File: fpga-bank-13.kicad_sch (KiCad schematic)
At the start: 1 part, among them U1 XC7K410T-2FFG900I

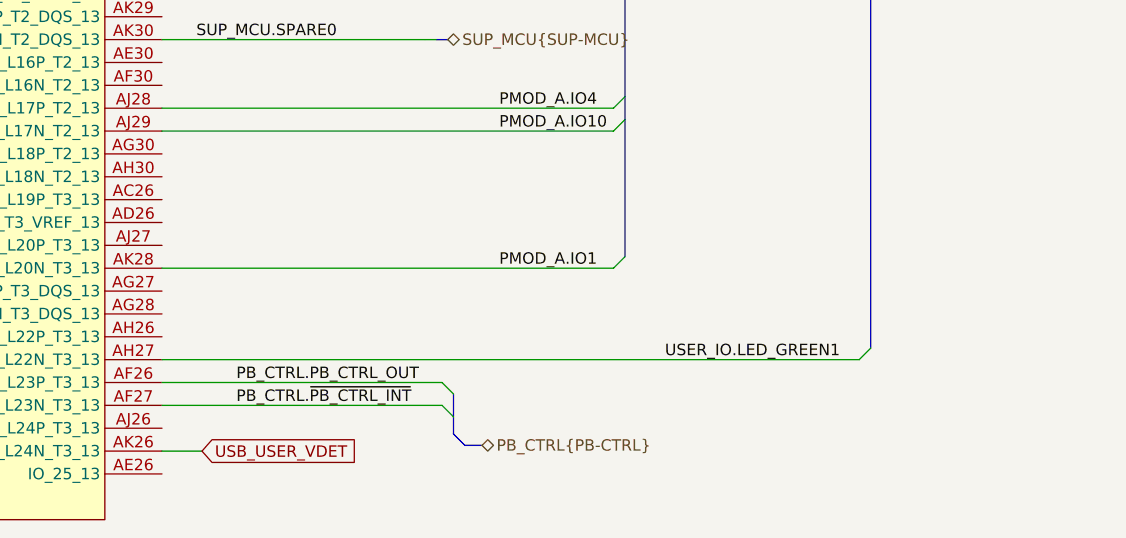
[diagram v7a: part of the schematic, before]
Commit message: Connected USB PON and DET signals to FPGA
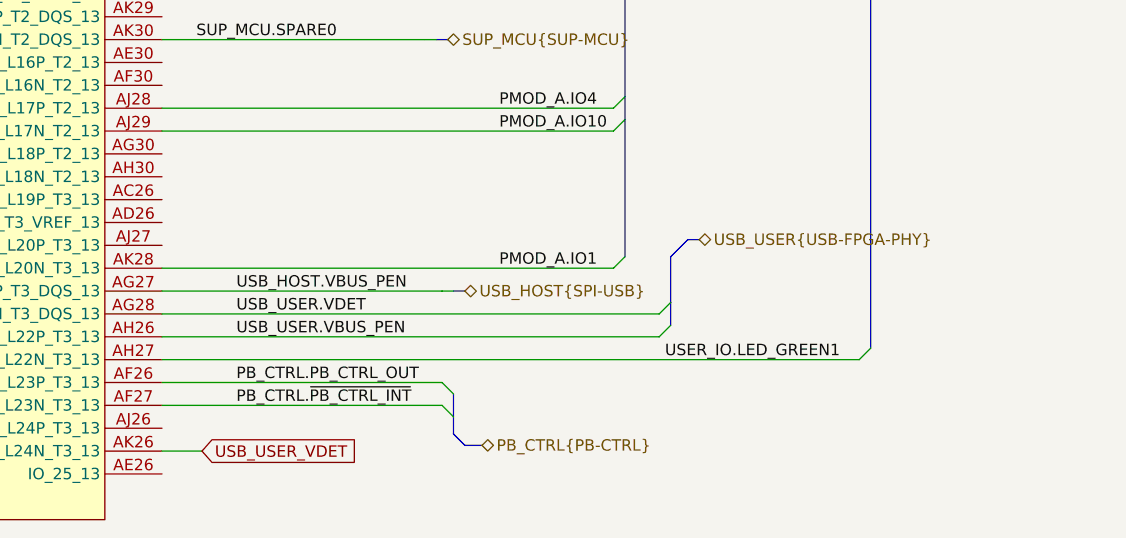
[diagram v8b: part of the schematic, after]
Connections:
- net USB_HOST.VBUS_PEN: now reaches U1.AG27 (IO_L21P_T3_DQS_13)
- net USB_USER.VDET: now reaches U1.AG28 (IO_L21N_T3_DQS_13)
- net USB_USER.VBUS_PEN: now reaches U1.AH26 (IO_L22P_T3_13)
